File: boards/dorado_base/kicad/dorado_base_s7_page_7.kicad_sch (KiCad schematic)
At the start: 26 parts

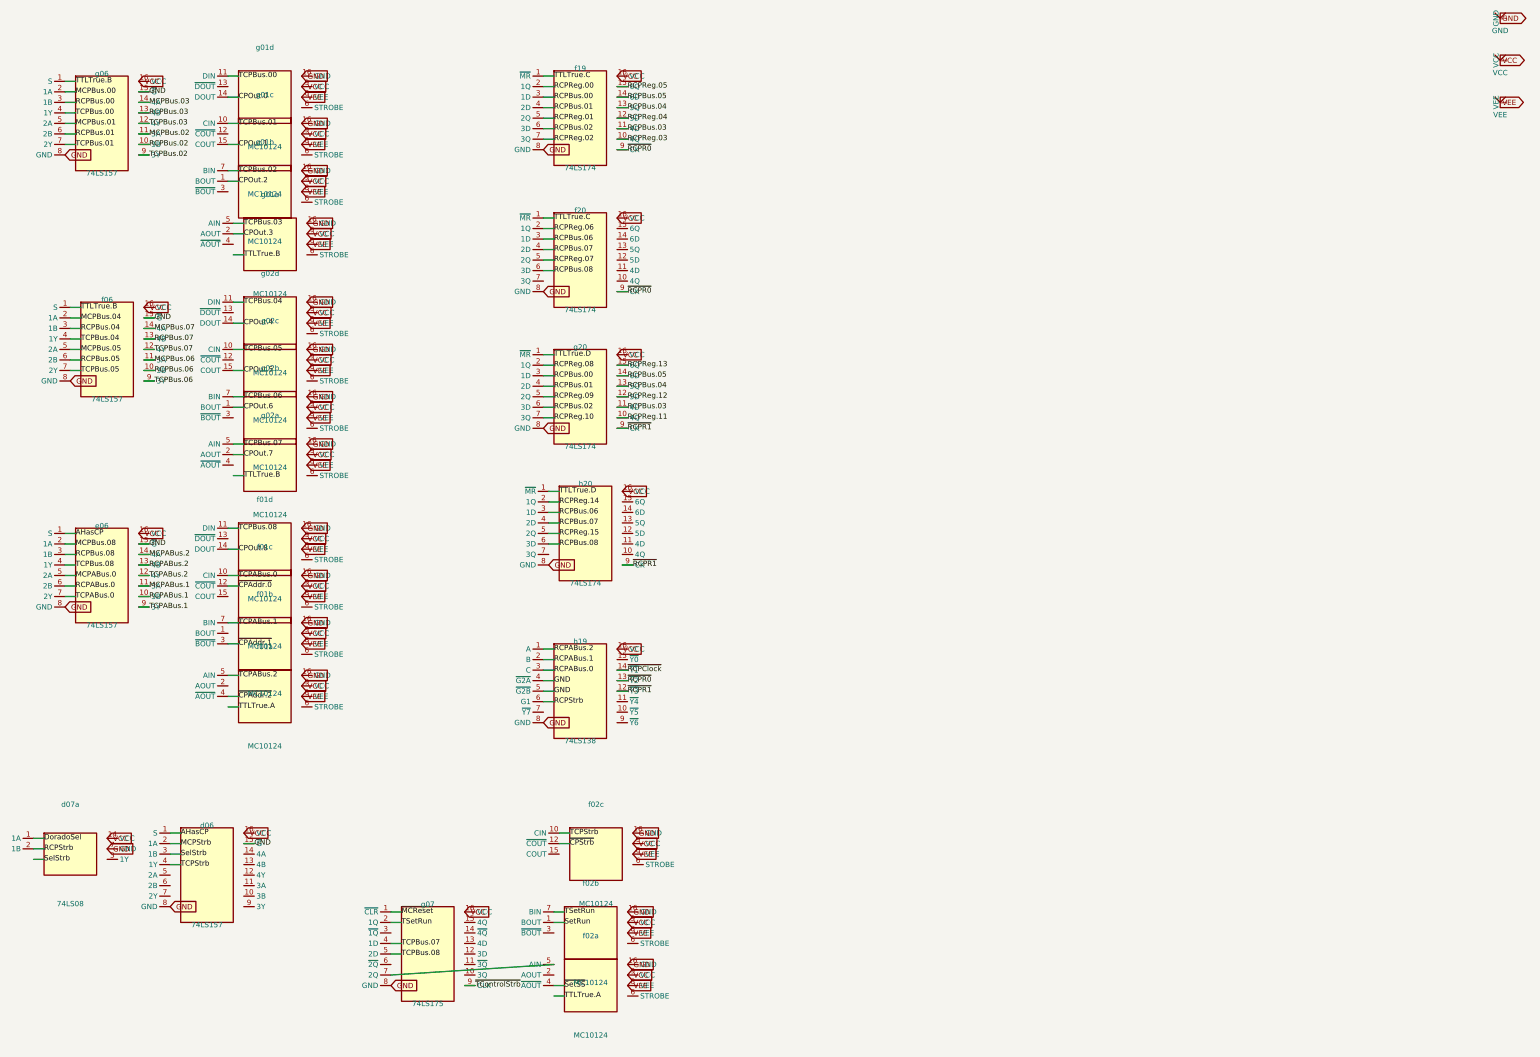
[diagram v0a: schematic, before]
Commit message: kicad export: faithful per-component symbols + path-aware wire routing
Switches the exporter from generic DIP symbols + straight-line pin-to-pin
wires to a per-component lib_symbol whose body matches the source bbox
and whose pins land at the placed pin_positions. The KiCad-rendered
schematic now reflects the original drawing's chip layout instead of an
auto-laid-out re-draw.

- synth_faithful_symbol(refdes, part, comp, scale): emits a unique
  user:_chip_<refdes> lib_symbol per component. Body shrunk by PIN_LENGTH
  on each side so pin lines extend visibly to the schematic dot. Pin
  (at) coords snapped to the 50-mil grid; angle picked from which body
  edge the pin is closest to.
- gen_sch chooses faithful when the component has pin_positions, else
  falls back to the existing generic synth_symbol path (so partly-
  transcribed sheets still export). pin_endpoint_mm in the faithful
  branch uses snapped local offsets so the absolute pin position equals
  instance_origin + offset, both grid-aligned (clears endpoint_off_grid).
- Wire emission: when net.path is set, emit one (wire) per consecutive
  polyline pair, snapped to grid. When absent, fall back to a one-corner
  Manhattan H-then-V route between each endpoint pair instead of a
  diagonal — gives KiCad something loadable until the tracer fills paths
  in. (Net path is consumed end-to-end through (wire (pts ...)).)
- Junctions: per-sheet sheets[].junctions emit (junction (at x y))
  blocks so KiCad's renderer draws connection dots where two wires
  cross AND connect.

Sheet 5 (full pin_positions, no split-gates) goes from
"blocking(35): endpoint_off_grid=11, power_pin_not_driven=24" to
PASS — only cross-sheet noise remains. Sheets 7 and 8 stay blocking=0
with their pre-existing pin_to_pin graph bugs unchanged.

Co-Authored-By: Claude Opus 4.7 (1M context) <noreply@anthropic.com>
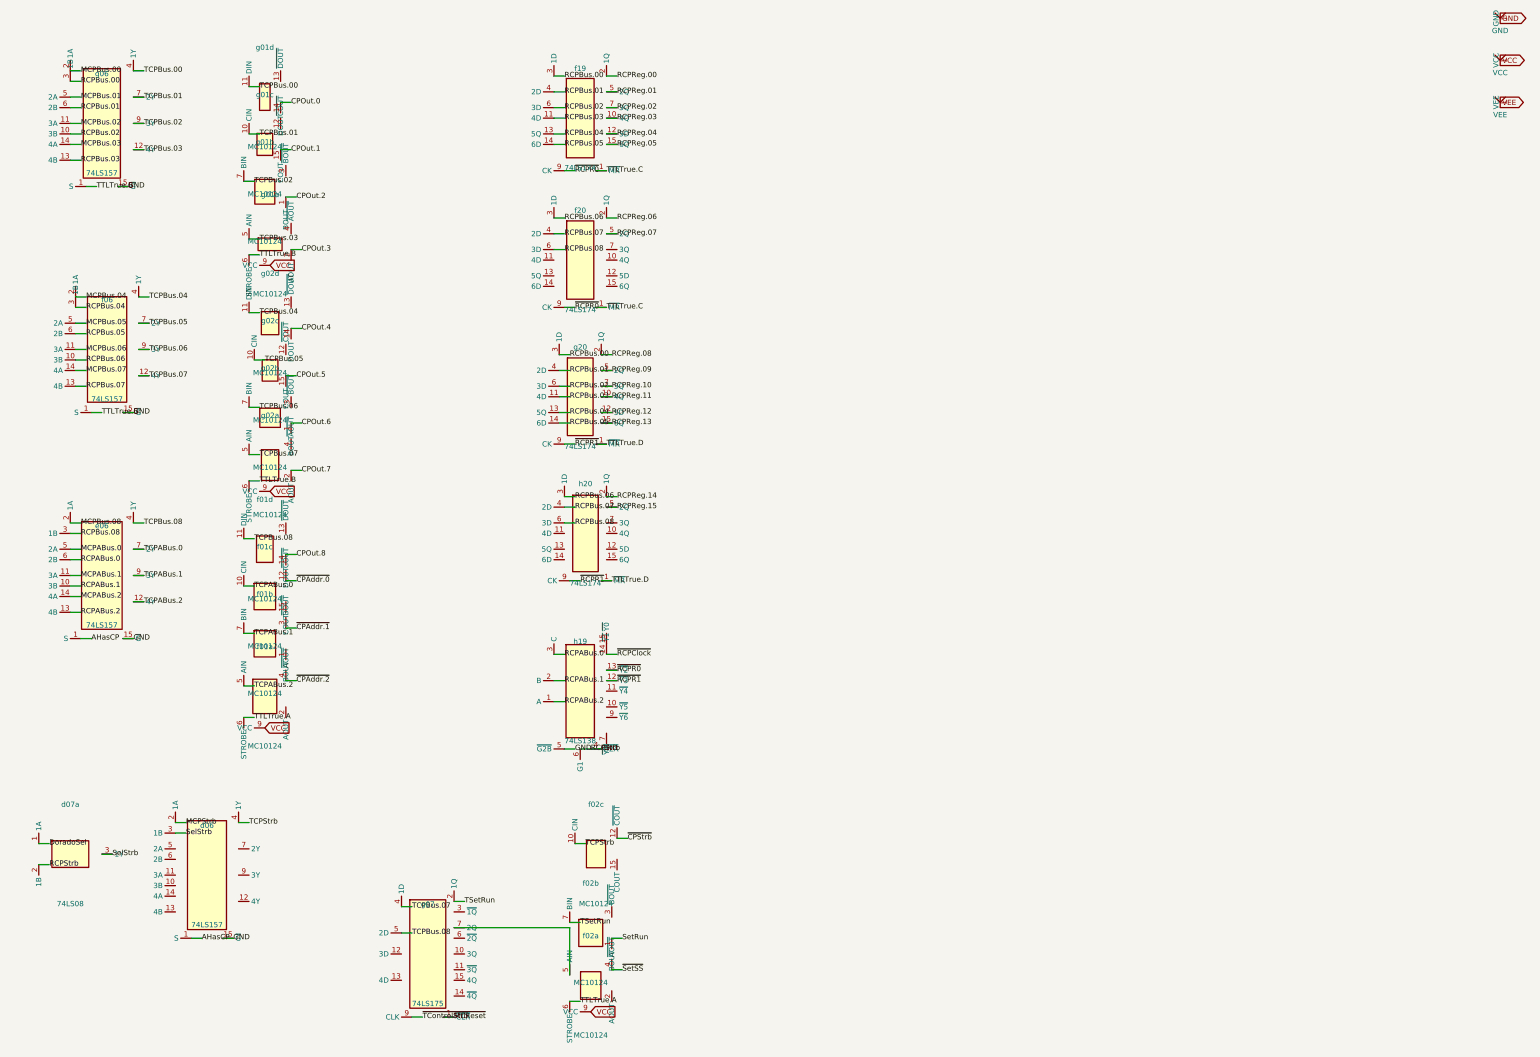
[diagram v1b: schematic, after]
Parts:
- d06: symbol user:74LS157 -> user:_chip_d06
- d07a: symbol user:74LS08_a -> user:_chip_d07a
- e06: symbol user:74LS157 -> user:_chip_e06
- f01a: symbol user:MC10124_a -> user:_chip_f01a
- f01b: symbol user:MC10124_b -> user:_chip_f01b
- f01c: symbol user:MC10124_c -> user:_chip_f01c
- f01d: symbol user:MC10124_d -> user:_chip_f01d
- f02a: symbol user:MC10124_a -> user:_chip_f02a
- f02b: symbol user:MC10124_b -> user:_chip_f02b
- f02c: symbol user:MC10124_c -> user:_chip_f02c
- f06: symbol user:74LS157 -> user:_chip_f06
- f19: symbol user:74LS174 -> user:_chip_f19
- f20: symbol user:74LS174 -> user:_chip_f20
- g01a: symbol user:MC10124_a -> user:_chip_g01a
- g01b: symbol user:MC10124_b -> user:_chip_g01b
- g01c: symbol user:MC10124_c -> user:_chip_g01c
- g01d: symbol user:MC10124_d -> user:_chip_g01d
- g02a: symbol user:MC10124_a -> user:_chip_g02a
- g02b: symbol user:MC10124_b -> user:_chip_g02b
- g02c: symbol user:MC10124_c -> user:_chip_g02c
- g02d: symbol user:MC10124_d -> user:_chip_g02d
- g06: symbol user:74LS157 -> user:_chip_g06
- g07: symbol user:74LS175 -> user:_chip_g07
- g20: symbol user:74LS174 -> user:_chip_g20
- h19: symbol user:74LS138 -> user:_chip_h19
- h20: symbol user:74LS174 -> user:_chip_h20
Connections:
- net RCPStrb is gone; now on net GND: d07a.2 (1B), h19.6 (G1)
- net GND: no longer d06.8 (GND), d07a.7 (GND), e06.8 (GND), f01a.16 (GND), f01b.16 (GND), f01c.16 (GND), f01d.16 (GND), f02a.16 (GND), f02b.16 (GND), f02c.16 (GND), f06.8 (GND), f19.8 (GND), f20.8 (GND), g01a.16 (GND), g01b.16 (GND), g01c.16 (GND), g01d.16 (GND), g02a.16 (GND), g02b.16 (GND), g02c.16 (GND), g02d.16 (GND), g06.8 (GND), g07.8 (GND), g20.8 (GND), h19.8 (GND), h20.8 (GND)
- net SelStrb: now also d07a.3 (1Y)
- net TTLTrue.A: now also f01a.6 (STROBE), f02a.6 (STROBE)
- net TTLTrue.B: now also g01a.6 (STROBE), g02a.6 (STROBE)
- net VCC: no longer d06.16 (VCC), d07a.14 (VCC), e06.16 (VCC), f01b.9 (VCC), f01c.9 (VCC), f01d.9 (VCC), f02b.9 (VCC), f02c.9 (VCC), f06.16 (VCC), f19.16 (VCC), f20.16 (VCC), g01b.9 (VCC), g01c.9 (VCC), g01d.9 (VCC), g02b.9 (VCC), g02c.9 (VCC), g02d.9 (VCC), g06.16 (VCC), g07.16 (VCC), g20.16 (VCC), h19.16 (VCC), h20.16 (VCC)
- net VEE: no longer f01a.8 (VEE), f01b.8 (VEE), f01c.8 (VEE), f01d.8 (VEE), f02a.8 (VEE), f02b.8 (VEE), f02c.8 (VEE), g01a.8 (VEE), g01b.8 (VEE), g01c.8 (VEE), g01d.8 (VEE), g02a.8 (VEE), g02b.8 (VEE), g02c.8 (VEE), g02d.8 (VEE)

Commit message: kicad export: fix pin-tip / polyline snap mismatch (1.27 mm off-grid)
Two code paths emitted absolute mm coords differently:

  pin tip   = _snap(M + cx_px*s) + _snap((ix-cx_px)*s)      # double-snap
  polyline  = _snap(M + p[0]*s)                              # single-snap

`_snap(a) + _snap(b) != _snap(a+b)` in general — the difference is 0 or
±1 grid unit. On Z80 SBC, a hand-traced wire from J1.2 to U1.14 had its
endpoint at the polyline's snapped coord (71.12, 76.20) while the pin
tip lived at the double-snapped coord (72.39, 74.93). KiCad reported
wire_dangling and 8 other short wires had the same workaround applied
(converted to label nets to dodge it).

Fix:
- synth_faithful_symbol now derives lib-symbol pin coords from the
  absolute pin tip (single-snap) minus the instance origin, instead of
  snapping the local offset directly. The local pin offset is no longer
  guaranteed to be a whole grid unit — body and pin can drift up to
  ~0.6 mm relative to each other — but the absolute pin tip is now
  always on grid AND agrees with every other coord-emitting path.
- gen_sch's faithful branch uses the same single-snap formula for
  pin_endpoint_mm.

This makes pin tips, polyline points, junctions, and discrete pins all
share one snap convention. Validated on Z80 SBC: RS232_TX (a workaround
label) converted back to wire + path produces wire_dangling=0.

Regression: dorado_base sheets 5/7/8, z80_sbc sheet 1, exidy_440 sheet 1
all stay blocking=0. Pre-existing graph wiring errors (pin_to_pin,
multiple_net_names) unchanged.

Removes bugs/polyline-pin-snap-mismatch.md.

Co-Authored-By: Claude Opus 4.7 (1M context) <noreply@anthropic.com>
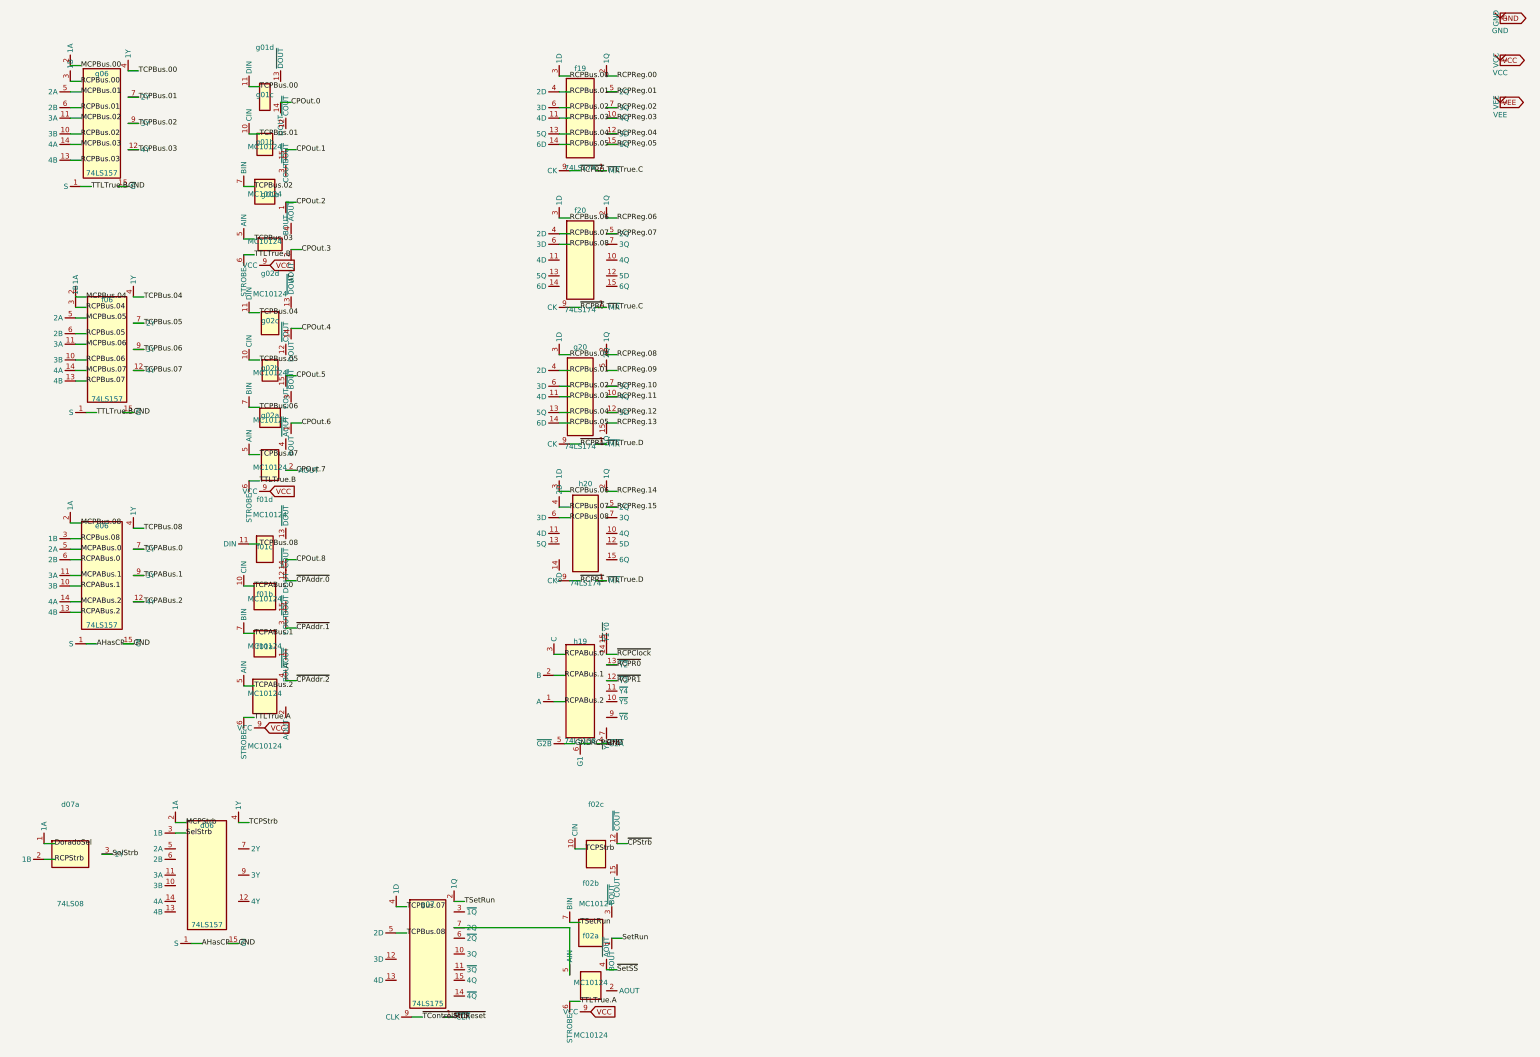
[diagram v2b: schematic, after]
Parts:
- d06, e06, f01a, f01b, f01c, f01d, f02a, f02b, f02c, f06, f19, f20, g01a, g01b, g01c, g01d, g02a, g02b, g02c, g02d, g06, g07, g20, h19, h20: footprint (none) -> Package_DIP:DIP-16_W7.62mm
- d07a: footprint (none) -> Package_DIP:DIP-14_W7.62mm
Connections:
- net GND: no longer d07a.2 (1B), h19.6 (G1)
- new net RCPStrb: d07a.2 (1B), h19.6 (G1)
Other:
- moved on the sheet: d06, d07a, e06, f01d, f02a, f02c, f06, f19, f20, g01a, g01b, g01c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
